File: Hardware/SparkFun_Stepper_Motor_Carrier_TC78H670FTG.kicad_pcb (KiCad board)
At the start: 4 copper layers, 15.2 x 20.3 mm, 34 parts, among them J1 Conn_01x08, J2 Conn_01x08

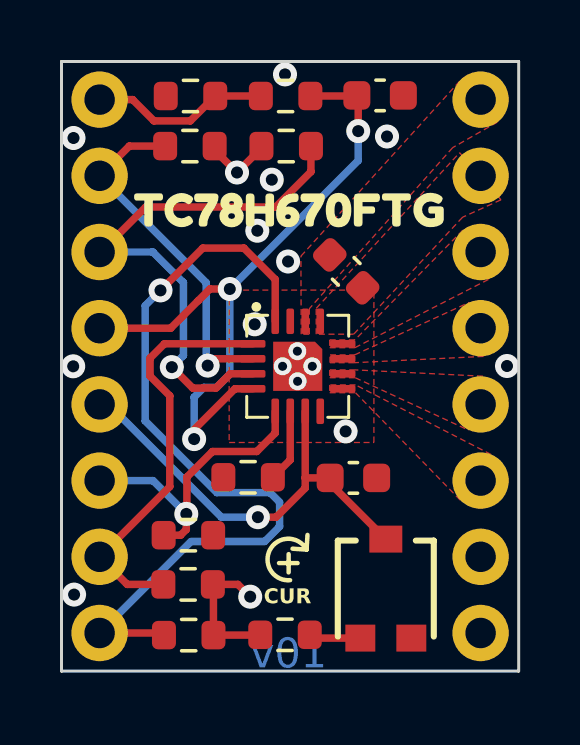
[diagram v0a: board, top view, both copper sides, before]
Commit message: review notes round 1
-SCH
--general cleanup
--fiducials
--section lines
--SFE logo
--OSHW logo
--voltage and current rating
--showing U1 reference and value
-BOARD
--flipped version number on board
--designer name
--ordering instructions
--CC license
--SFE logo
--oshw logo
--polygon clearnaces set to 0.2032mm
--removed unncessary gnd vias
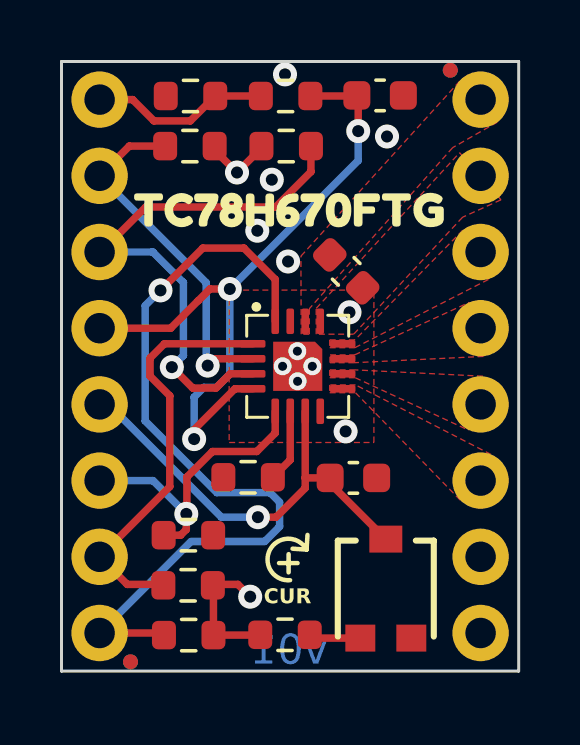
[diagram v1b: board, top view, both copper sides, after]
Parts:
- added FID1: Fiducial_0.5mm, SparkFun-Aesthetic:Fiducial_0.5mm_Mask1mm, F.Cu at (147.6, 94.3)
- added FID2: Fiducial_0.5mm, SparkFun-Aesthetic:Fiducial_0.5mm_Mask1mm, B.Cu at (147.6, 94.3)
- added FID3: Fiducial_0.5mm, SparkFun-Aesthetic:Fiducial_0.5mm_Mask1mm, B.Cu at (136.9, 114.0)
- added FID4: Fiducial_0.5mm, SparkFun-Aesthetic:Fiducial_0.5mm_Mask1mm, F.Cu at (136.9, 114.0)
- added G***: LOGO, SparkFun-Aesthetic:SparkFun_Logo_7mm, B.Cu at (141.6, 98.4)
- added G1: OSHW_Logo, SparkFun-Aesthetic:Creative_Commons_License, F.Cu at (82.6, 85.2)
- added Ref**: Val**, SparkFun-Aesthetic:OSHW_Logo_2.5mm, B.Cu at (142.9, 111.7)
- added U2: ~, SparkFun-Aesthetic:ORDERING_INSTRUCTIONS, F.Cu at (167.6, 61.0)
- U1: value ~ -> TC78H670FTG
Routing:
- net GND: vias 15 -> 11
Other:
- board text added: "Finish: HASL Lead Free"
- board text added: "Layers: 4"
- board text added: "P. Lewis"
- board text added: "Solder Mask: Red"
- board text added: "Thickness: 1.6mm"
